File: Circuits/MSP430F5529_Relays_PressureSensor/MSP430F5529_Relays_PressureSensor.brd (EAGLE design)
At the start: 58.4 x 68.3 mm, 8 parts, among them K1 AQV21SMD, K2 AQV21SMD, U1 SSCDANT030PG2A3

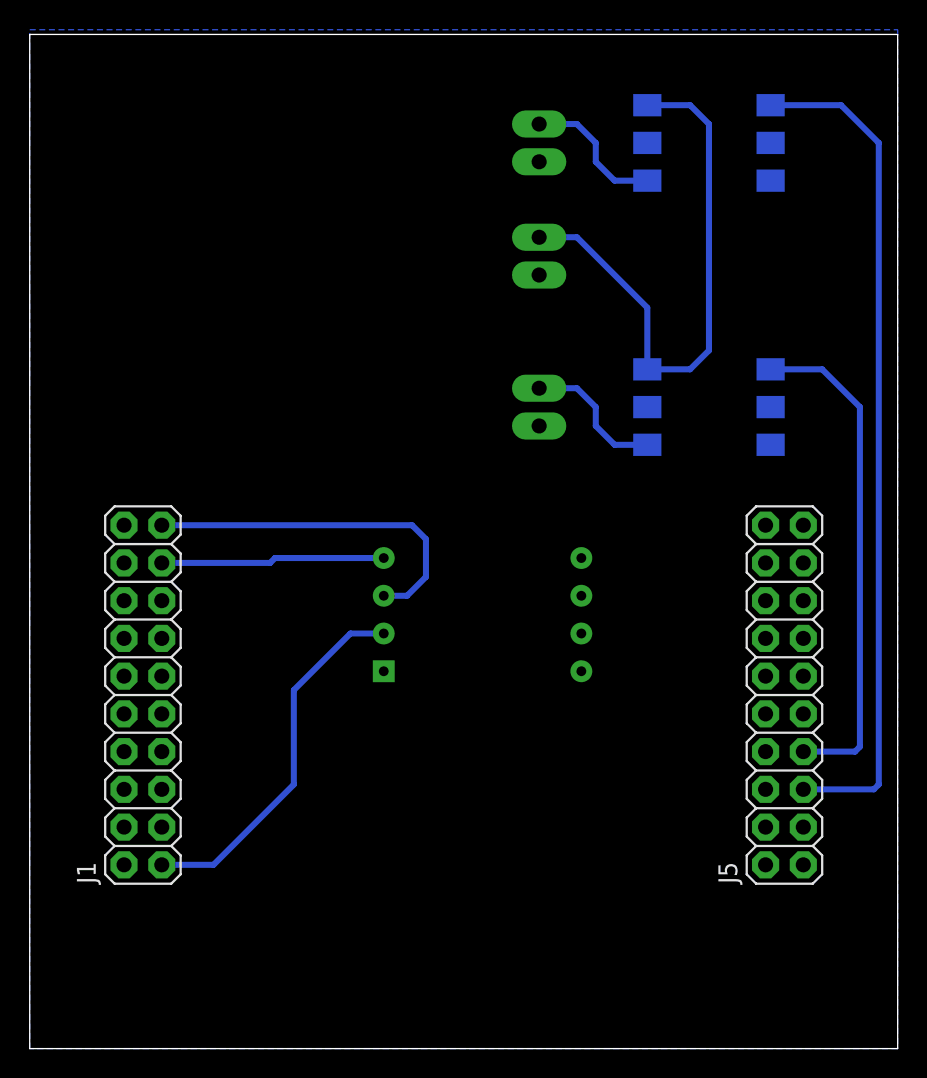
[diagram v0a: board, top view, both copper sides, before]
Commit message: Fix error on pressure board (launchpad header rotated 180 )
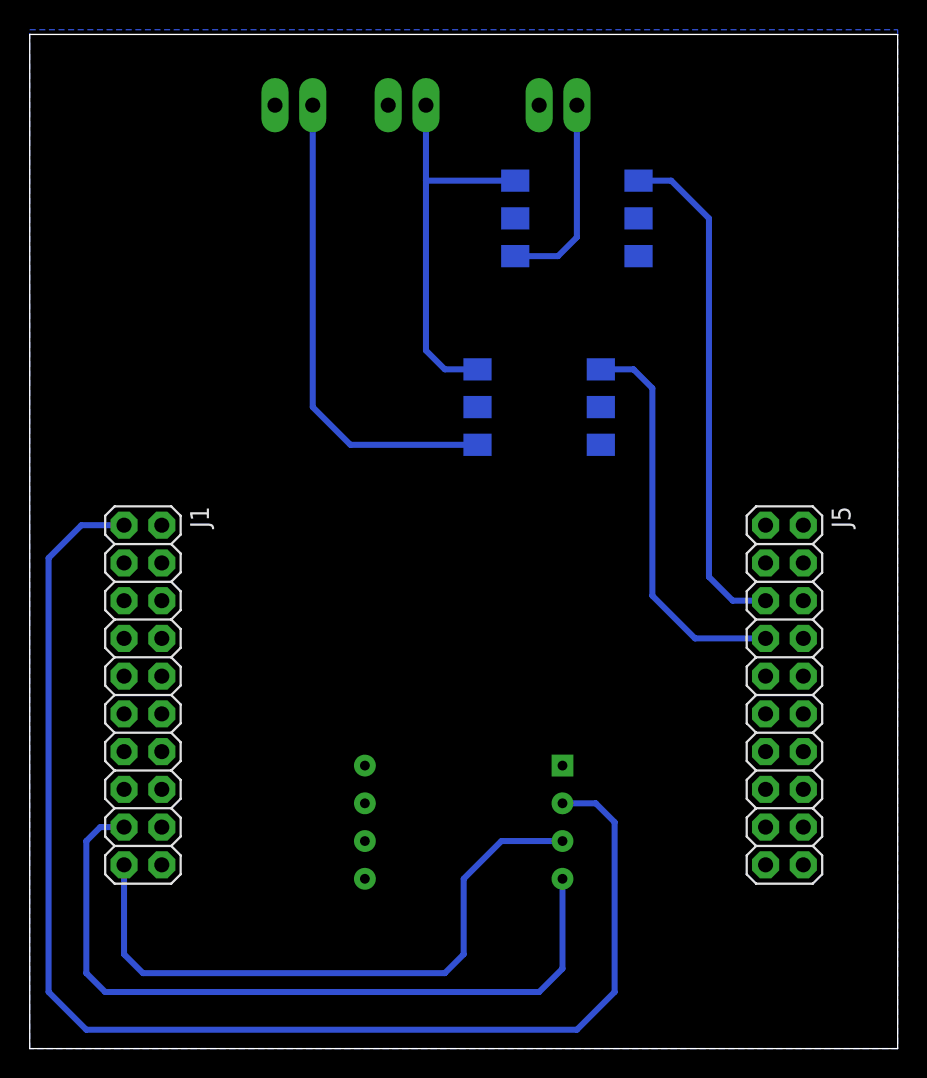
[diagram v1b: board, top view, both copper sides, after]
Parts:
- moved JP2 27.3 mm to (17.8, 67.3), turned to 0 degrees
- moved JP1 14.9 mm to (25.4, 67.3), turned to 0 degrees
- moved U1 14.0 mm to (29.2, 15.2), turned to 0 degrees
- moved K1 11.4 mm to (34.3, 43.2)
- moved K2 10.2 mm to (36.8, 55.9)
- moved JP3 8.13 mm to (35.6, 67.3), turned to 0 degrees
- turned J1 to 270 degrees
- turned J5 to 270 degrees
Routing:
- net 3V3: track 25.1 -> 90.9 mm
- net P4.2: track 15.1 -> 51.1 mm
- net INFLATE_PWR: track 9.60 -> 32.5 mm
- net P1.5: track 56.7 -> 34.4 mm
- net P4.1: track 24.4 -> 42.7 mm
- net 12V: track 38.0 -> 26.5 mm
- net P1.4: track 33.9 -> 26.8 mm
- net DEFLATE_PWR: track 9.60 -> 13.6 mm

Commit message: add pullup resistors to I2C lines
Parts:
- added R1, R2: 1k, resistor:M1206
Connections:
- net 3V3: now also R1.2, R2.2
- net P4.1: now also R1.1
- net P4.2: now also R2.1
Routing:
- net P4.2: track 51.1 -> 54.5 mm
- net P4.1: track 42.7 -> 46.1 mm
- net 3V3: track 90.9 -> 94.0 mm
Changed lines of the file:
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@@
 <layer number="97" name="Info" color="7" fill="1" visible="no" active="no"/>
 <layer number="98" name="Guide" color="6" fill="1" visible="no" active="no"/>
+<layer number="99" name="SpiceOrder" color="5" fill="1" visible="no" active="no"/>
 </layers>
 <board>
@@
 <attribute name="VALUE" x="22.86" y="20.32" size="1.27" layer="28" rot="MR0" align="center"/>
 </element>
+<element name="R1" library="resistor" library_urn="urn:adsk.eagle:library:348" package="M1206" package3d_urn="urn:adsk.eagle:package:26088/1" value="1k" x="40.64" y="13.97" smashed="yes" rot="MR180">
+<attribute name="NAME" x="39.37" y="12.7" size="1.27" layer="26" rot="MR180"/>
+<attribute name="VALUE" x="39.37" y="16.51" size="1.27" layer="28" rot="MR180"/>
+</element>
+<element name="R2" library="resistor" library_urn="urn:adsk.eagle:library:348" package="M1206" package3d_urn="urn:adsk.eagle:package:26088/1" value="1k" x="40.64" y="8.89" smashed="yes" rot="MR180">
+<attribute name="NAME" x="39.37" y="7.62" size="1.27" layer="26" rot="MR180"/>
+<attribute name="VALUE" x="39.37" y="11.43" size="1.27" layer="28" rot="MR180"/>
+</element>
 </elements>
 <signals>
@@
 <contactref element="J1" pad="1"/>
 <contactref element="U1" pad="2"/>
+<contactref element="R2" pad="2"/>
+<contactref element="R1" pad="2"/>
+<wire x1="42.04" y1="8.89" x2="42.04" y2="13.97" width="0.4064" layer="16"/>
+<wire x1="42.04" y1="13.97" x2="42.04" y2="16.38" width="0.4064" layer="16"/>
+<wire x1="42.04" y1="16.38" x2="41.91" y2="16.51" width="0.4064" layer="16"/>
+<wire x1="41.91" y1="16.51" x2="35.86" y2="16.51" width="0.4064" layer="16"/>
 <wire x1="6.35" y1="35.2298" x2="3.4798" y2="35.2298" width="0.4064" layer="16"/>
-<wire x1="1.27" y1="33.02" x2="1.27" y2="3.81" width="0.4064" layer="16"/>
-<wire x1="1.27" y1="3.81" x2="3.81" y2="1.27" width="0.4064" layer="16"/>
-<wire x1="3.81" y1="1.27" x2="36.83" y2="1.27" width="0.4064" layer="16"/>
-<wire x1="36.83" y1="1.27" x2="39.37" y2="3.81" width="0.4064" layer="16"/>
-<wire x1="39.37" y1="15.24" x2="38.1" y2="16.51" width="0.4064" layer="16"/>
-<wire x1="38.1" y1="16.51" x2="35.86" y2="16.51" width="0.4064" layer="16"/>
-<wire x1="3.4798" y1="35.2298" x2="1.27" y2="33.02" width="0.4064" layer="16"/>
-<wire x1="39.37" y1="3.81" x2="39.37" y2="15.24" width="0.4064" layer="16"/>
+<wire x1="3.4798" y1="35.2298" x2="2.54" y2="34.29" width="0.4064" layer="16"/>
+<wire x1="2.54" y1="34.29" x2="2.54" y2="3.81" width="0.4064" layer="16"/>
+<wire x1="42.04" y1="3.94" x2="42.04" y2="8.89" width="0.4064" layer="16"/>
+<wire x1="6.35" y1="2.54" x2="7.62" y2="2.54" width="0.4064" layer="16"/>
+<wire x1="7.62" y1="2.54" x2="40.64" y2="2.54" width="0.4064" layer="16"/>
+<wire x1="40.64" y1="2.54" x2="42.04" y2="3.94" width="0.4064" layer="16"/>
+<wire x1="2.54" y1="3.81" x2="3.81" y2="2.54" width="0.4064" layer="16"/>
+<wire x1="3.81" y1="2.54" x2="6.35" y2="2.54" width="0.4064" layer="16"/>
 </signal>
 <signal name="5V">
@@
 <wire x1="31.75" y1="13.97" x2="29.21" y2="11.43" width="0.4064" layer="16"/>
 <wire x1="29.21" y1="11.43" x2="29.21" y2="6.35" width="0.4064" layer="16"/>
+<contactref element="R1" pad="1"/>
+<wire x1="39.24" y1="13.97" x2="35.86" y2="13.97" width="0.4064" layer="16"/>
 </signal>
 <signal name="P3.5">
@@
 <wire x1="3.81" y1="5.08" x2="5.08" y2="3.81" width="0.4064" layer="16"/>
 <wire x1="5.08" y1="3.81" x2="34.29" y2="3.81" width="0.4064" layer="16"/>
-<wire x1="35.86" y1="11.43" x2="35.86" y2="5.38" width="0.4064" layer="16"/>
+<wire x1="35.86" y1="11.43" x2="35.86" y2="8.89" width="0.4064" layer="16"/>
+<wire x1="35.86" y1="8.89" x2="35.86" y2="5.38" width="0.4064" layer="16"/>
 <wire x1="35.86" y1="5.38" x2="34.29" y2="3.81" width="0.4064" layer="16"/>
+<contactref element="R2" pad="1"/>
+<wire x1="39.24" y1="8.89" x2="35.86" y2="8.89" width="0.4064" layer="16"/>
 </signal>
 <signal name="P8.2">

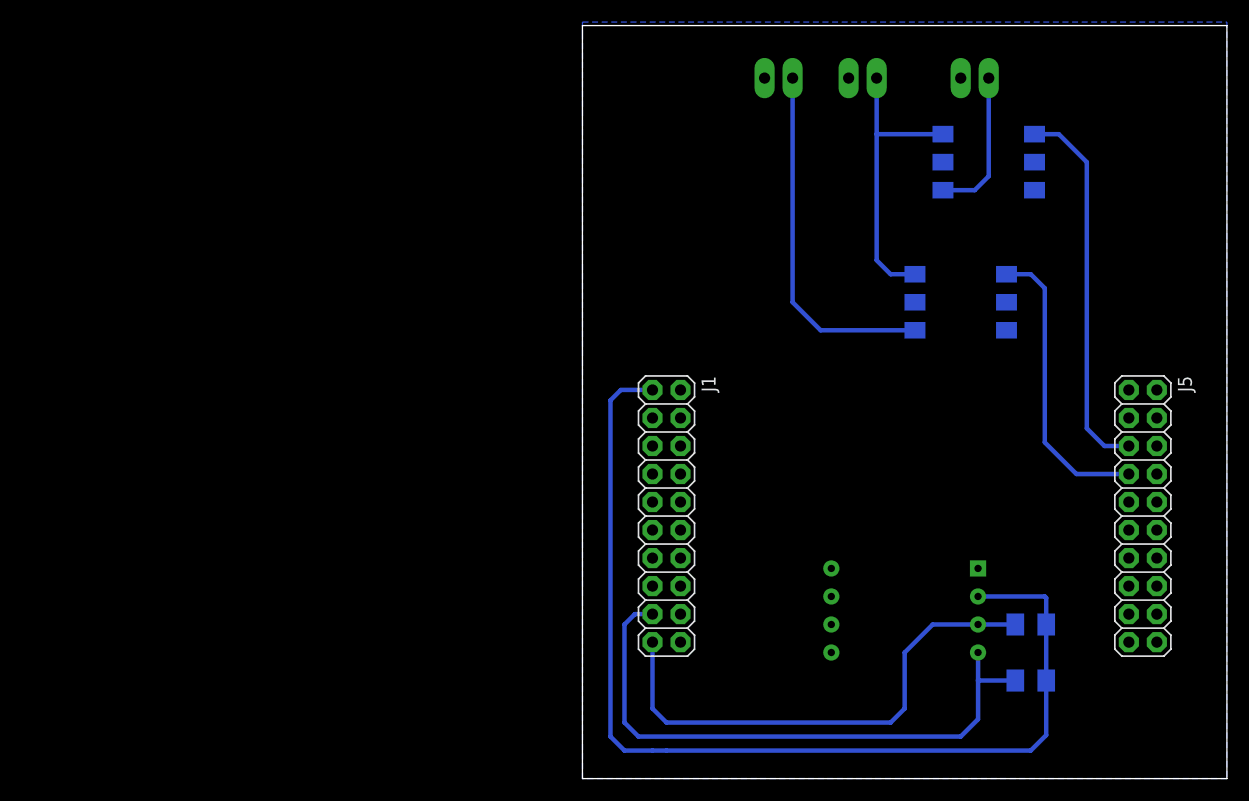
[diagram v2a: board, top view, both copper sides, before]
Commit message: Substitute right angle pressure sensor
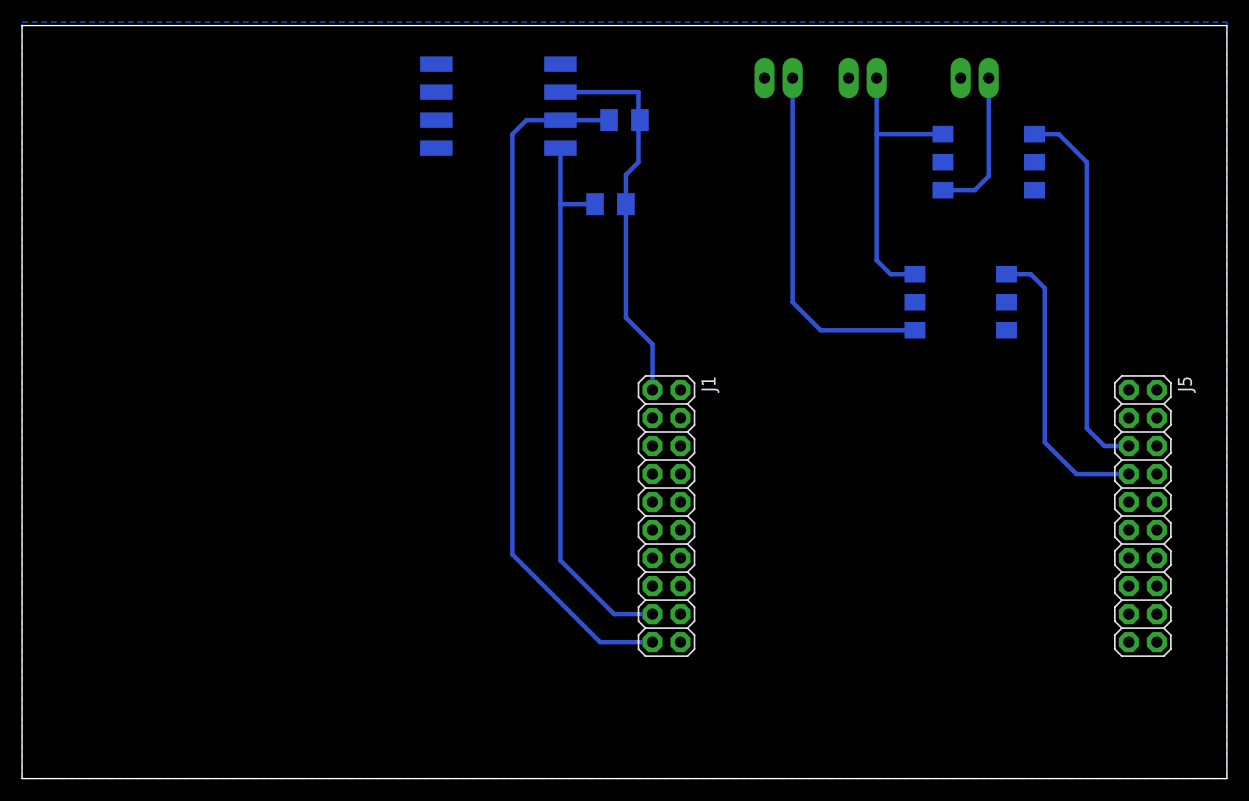
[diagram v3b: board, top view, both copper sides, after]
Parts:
- removed U1: SSCDANT030PG2A3, SamacSys_Parts:DIP1330W46P254L1000H1375Q8N
- added U2: SSCMRNN015PA3A3, SamacSys_Parts:SOP254P1330X598-8N
- moved R1 58.7 mm to (3.81, 59.7)
- moved R2 57.6 mm to (2.54, 52.1)
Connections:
- net 3V3: now also U2.2; no longer U1.2
- net GND: now also U2.1; no longer U1.1
- net P4.1: now also U2.3; no longer U1.3
- net P4.2: now also U2.4; no longer U1.4
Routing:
- net 3V3: track 94.0 -> 35.7 mm
- net P4.1: track 46.1 -> 63.4 mm
- net P4.2: track 54.5 -> 50.9 mm
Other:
- board size 58.4 x 68.3 mm -> 109.2 x 68.3 mm

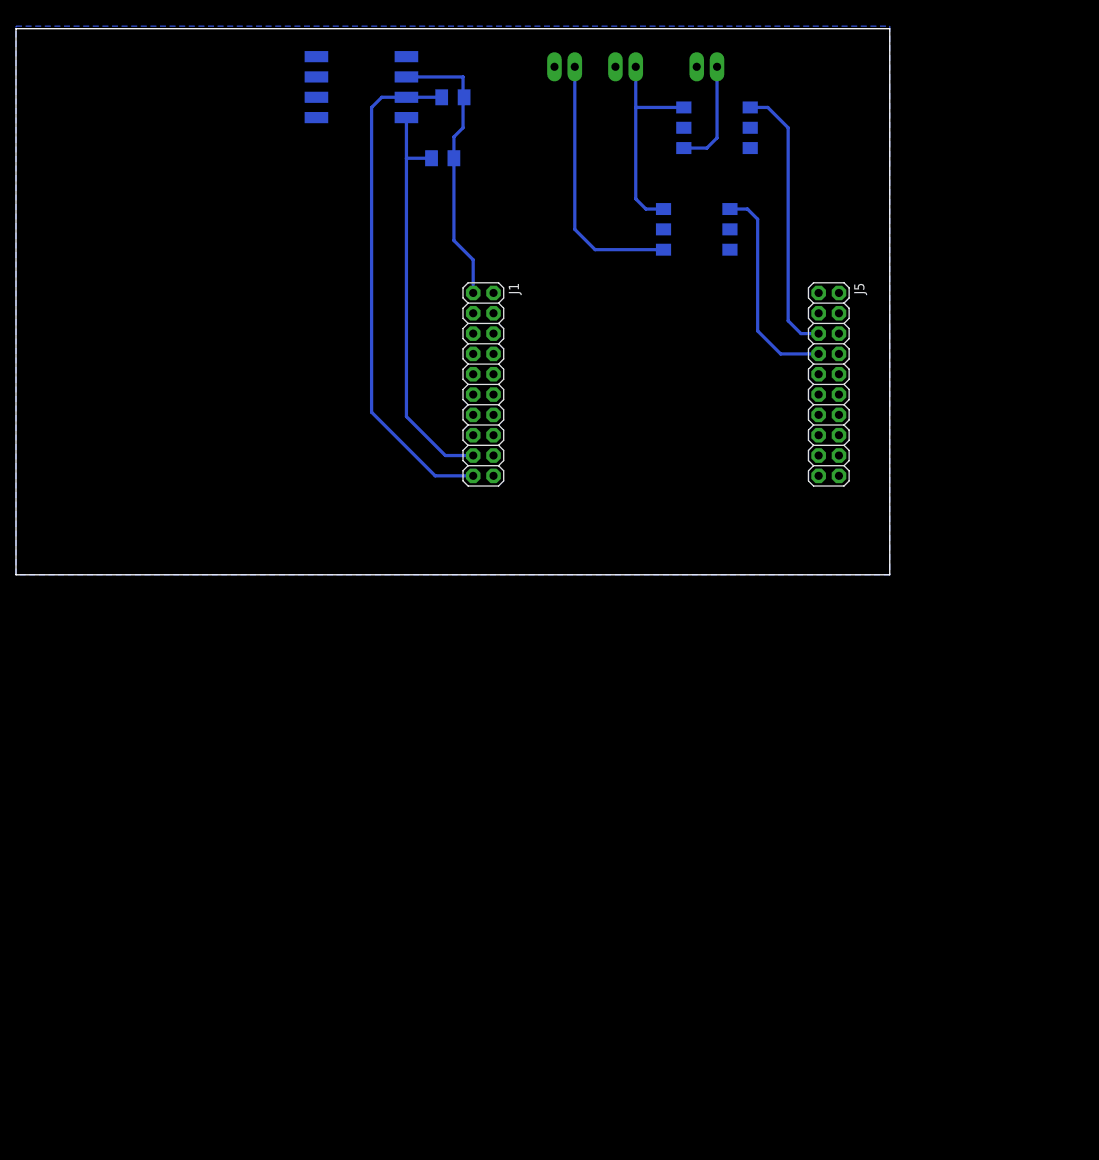
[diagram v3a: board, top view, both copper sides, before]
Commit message: Add switches for control of LCD instead of touchscreen
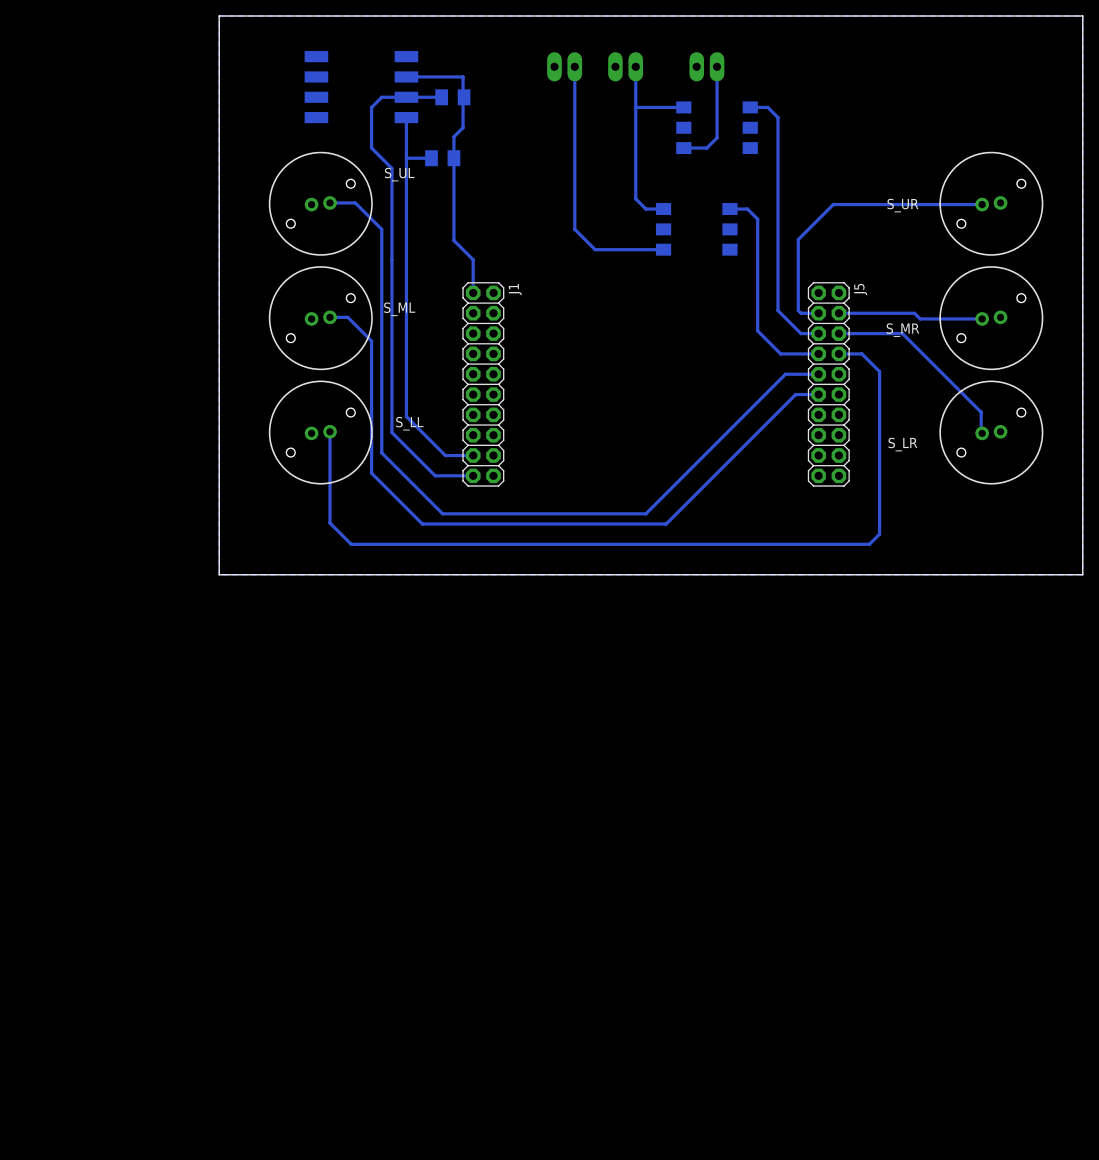
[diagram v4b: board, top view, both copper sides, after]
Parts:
- added S_LL, S_LR, S_ML, S_MR, S_UL, S_UR: K12C15N, SamacSys_Parts:K12C15N
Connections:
- new net P1.2: J5.11, S_ML.2
- new net P1.3: J5.9, S_UL.2
- new net P2.0: J5.4, S_MR.2
- new net P2.2: J5.6, S_LR.2
- new net P2.4: J5.3, S_UR.2
- new net P7.4: J5.8, S_LL.2
- net GND: now also S_LL.1, S_LR.1, S_ML.1, S_MR.1, S_UL.1, S_UR.1
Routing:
- net P7.4: track 0.00 -> 108.1 mm
- net P1.3: track 0.00 -> 100.8 mm
- net P1.2: track 0.00 -> 88.2 mm
- net P2.4: track 0.00 -> 36.4 mm
- net P2.2: track 0.00 -> 24.5 mm
- net P2.0: track 0.00 -> 18.2 mm
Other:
- board size 109.2 x 68.3 mm -> 107.9 x 69.8 mm
